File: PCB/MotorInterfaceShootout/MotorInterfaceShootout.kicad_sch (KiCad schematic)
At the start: 0 parts

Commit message: main schem start
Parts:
- added C1, C2, C3: 1uF, TJR:C_Rect_L7.3mm_W4.5_H9.5mm_P5.0mmx, symbol Device:C
- added D1, D2: LED, TSL:LED_D3.0mm, symbol 00TJR:LED
- added D3, D4, D5, D6, D7: 3V, symbol TJR:ZENER
- added J1: Motor Connector, Connector_JST:JST_XH_B6B-XH-A_1x06_P2.50mm_Vertical, symbol Connector:Conn_01x06_Pin
- added J3: Screw_Terminal_01x10, symbol connector:Screw_Terminal_01x10
- added R10, R11, R12, R7, R8, R9: 10k, TJR:R_Axial_DIN0207_L6.3mm_D2.5mm_P7.62mm_Horizontal, symbol TJR:R
- added R14, R16: 5.1k, TJR:R_Axial_DIN0207_L6.3mm_D2.5mm_P7.62mm_Horizontal, symbol TJR:R
- added R15: 47k, TJR:R_Axial_DIN0207_L6.3mm_D2.5mm_P7.62mm_Horizontal, symbol TJR:R
- added R18, R19, R20, R21: 1.3k, TJR:R_Axial_DIN0207_L6.3mm_D2.5mm_P7.62mm_Horizontal, symbol TJR:R
- added R22: 6.8k, TJR:R_Axial_DIN0207_L6.3mm_D2.5mm_P7.62mm_Horizontal, symbol TJR:R
- added R23: 1k, TJR:R_Axial_DIN0207_L6.3mm_D2.5mm_P7.62mm_Horizontal, symbol TJR:R
- added R5, R6: 330, TJR:R_Axial_DIN0207_L6.3mm_D2.5mm_P7.62mm_Horizontal, symbol TJR:R
- added U1: Pico, TJR:RPi_Pico_SMD_TH, symbol MCU_RaspberryPi_and_Boards:Pico
- added U2: OPA4197, TJR:D14_TEX, symbol Amplifier_Operational:OPA4197xPW
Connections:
- new net: R11.1, R8.2, U2.6 (-)
- new net: J3.1 (Pin_1), R21.1
- new net: R10.1, R7.2, U2.2 (-)
- new net: J3.3 (Pin_3), R22.1
- new net: J3.2 (Pin_2), R20.1
- new net: J3.4 (Pin_4), R18.1
- new net: J3.5 (Pin_5), R19.1
- new net: R12.1, R9.2, U2.9 (-)
- new net: R15.1, U2.7
- new net: R16.1, U2.8
- new net: D2.2 (A), R6.2
- new net: D1.2 (A), R5.2
- new net: R14.1, U2.1
- new net +3.3V: R7.1, R8.1, R9.1, U1.36 (3V3)
- new net +5V: U1.39 (VSYS)
- new net A: J1.5 (Pin_5), U1.4 (GPIO2)
- new net A0: D4.1 (K), R20.2
- new net A1: D6.1 (K), R21.2
- new net Analog Position: C3.1, R16.2
- new net Analog Position x10: C1.1, R14.2
- new net Analog Speed: C2.1, R15.2
- new net B: J1.6 (Pin_6), U1.5 (GPIO3)
- new net E+: J1.3 (Pin_3)
- new net E-: J1.4 (Pin_4)
- new net GND: C1.2, C2.2, C3.2, D1.1 (K), D2.1 (K), D3.2 (A), D4.2 (A), D5.2 (A), D6.2 (A), D7.2 (A), J3.9 (Pin_9), R10.2, R11.2, R12.2, R23.2, U1.12 (GPIO9), U1.18 (GND), U1.23 (GND), U1.28 (GND), U1.33 (AGND), U1.38 (GND), U1.8 (GND)
- new net M+: J1.1 (Pin_1)
- new net M-: J1.2 (Pin_2)
- new net PIN_FWD: R5.1, U1.21 (GPIO16)
- new net PIN_HOME_CMD: D5.1 (K), R18.2, U1.20 (GPIO15)
- new net PIN_HOME_LIMIT: D3.1 (K), R19.2, U1.19 (GPIO14)
- new net PIN_MOTOR_SEL: U1.17 (GPIO13)
- new net PIN_PWM_POS: J3.7 (Pin_7), U1.24 (GPIO18), U2.10 (+)
- new net PIN_PWM_POSX10: J3.6 (Pin_6), U1.26 (GPIO20), U2.3 (+)
- new net PIN_PWM_SPD: J3.8 (Pin_8), U1.25 (GPIO19), U2.5 (+)
- new net PIN_PWM_SPD_CMD: U1.27 (GPIO21)
- new net PIN_REV: R6.1, U1.22 (GPIO17)
- new net PIN_SPD_CAL_ADC: U1.32 (GPIO27_ADC1)
- new net PIN_SPD_CMD_ADC: D7.1 (K), R22.2, R23.1, U1.31 (GPIO26_ADC0)
- new net VSYS: J3.10 (Pin_10)
- no-connect marks 0 -> 21
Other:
- added sheet H-Bridge (h-bridge.kicad_sch)
- added sheet Power (power.kicad_sch)
- note added: "Main Interface Terminals Power / PLC / Limit Switch"
- note added: "Motor / Encoder Connector"
- note added: "PWM Level Transition and Integration to Analog DC Voltage 0 - 10V"
- note added: "Raspberry Pi PICO Note: Place decouple near VSYS"

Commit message: fix power
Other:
- moved on the sheet: D1, D2, R5, R6
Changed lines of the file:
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@@
 	(wire
 		(pts
-			(xy 410.21 110.49) (xy 410.21 111.76)
+			(xy 149.86 151.13) (xy 149.86 152.4)
 		)
 		(stroke
@@
 	(wire
 		(pts
-			(xy 416.56 119.38) (xy 416.56 120.65)
+			(xy 156.21 160.02) (xy 156.21 161.29)
 		)
 		(stroke
@@
 	(wire
 		(pts
-			(xy 416.56 96.52) (xy 416.56 102.87)
+			(xy 156.21 137.16) (xy 156.21 143.51)
 		)
 		(stroke
@@
 	(wire
 		(pts
-			(xy 410.21 119.38) (xy 410.21 120.65)
+			(xy 149.86 160.02) (xy 149.86 161.29)
 		)
 		(stroke
@@
 	(wire
 		(pts
-			(xy 407.67 100.33) (xy 410.21 100.33)
+			(xy 147.32 140.97) (xy 149.86 140.97)
 		)
 		(stroke
@@
 	(wire
 		(pts
-			(xy 407.67 96.52) (xy 416.56 96.52)
+			(xy 147.32 137.16) (xy 156.21 137.16)
 		)
 		(stroke
@@
 	(wire
 		(pts
-			(xy 410.21 100.33) (xy 410.21 102.87)
+			(xy 149.86 140.97) (xy 149.86 143.51)
 		)
 		(stroke
@@
 	(wire
 		(pts
-			(xy 416.56 110.49) (xy 416.56 111.76)
+			(xy 156.21 151.13) (xy 156.21 152.4)
 		)
 		(stroke
@@
 	(global_label "PIN_REV"
 		(shape input)
-		(at 407.67 96.52 180)
+		(at 147.32 137.16 180)
 		(fields_autoplaced yes)
 		(effects
@@
 		)
 		(property "Intersheetrefs" "${INTERSHEET_REFS}"
-			(at 397.0043 96.52 0)
+			(at 136.6543 137.16 0)
 			(effects
 				(font
@@
 	(global_label "PIN_FWD"
 		(shape input)
-		(at 407.67 100.33 180)
+		(at 147.32 140.97 180)
 		(fields_autoplaced yes)
 		(effects
@@
 		)
 		(property "Intersheetrefs" "${INTERSHEET_REFS}"
-			(at 396.7019 100.33 0)
+			(at 136.3519 140.97 0)
 			(effects
 				(font
@@
 				)
 				(justify left)
-				(hide yes)
 			)
 		)
@@
 				)
 				(justify left)
-				(hide yes)
 			)
 		)
@@
 	(symbol
 		(lib_id "TJR:R")
-		(at 416.56 106.68 0)
+		(at 156.21 147.32 0)
 		(unit 1)
 		(exclude_from_sim no)
@@
 		(dnp no)
 		(property "Reference" "R6"
-			(at 417.83 105.4099 0)
+			(at 157.48 146.0499 0)
 			(effects
 				(font
@@
 		)
 		(property "Value" "330"
-			(at 417.83 107.9499 0)
+			(at 157.48 148.5899 0)
 			(effects
 				(font
@@
 		)
 		(property "Footprint" "TJR:R_Axial_DIN0207_L6.3mm_D2.5mm_P7.62mm_Horizontal"
-			(at 414.782 106.68 90)
+			(at 154.432 147.32 90)
 			(effects
 				(font
@@
 		)
 		(property "Datasheet" "https://www.seielect.com/catalog/sei-cf_cfm.pdf"
-			(at 416.56 106.68 0)
+			(at 156.21 147.32 0)
 			(effects
 				(font
@@
 		)
 		(property "Description" "1/2W"
-			(at 416.56 106.68 0)
+			(at 156.21 147.32 0)
 			(effects
 				(font
@@
 		)
 		(property "digikey" "https://www.digikey.com/en/products/detail/stackpole-electronics-inc/CFM12JT47R0/1741962"
-			(at 416.56 106.68 0)
+			(at 156.21 147.32 0)
 			(effects
 				(font
@@
 		)
 		(property "Cost (ea.)" ""
-			(at 416.56 106.68 0)
+			(at 156.21 147.32 0)
 			(effects
 				(font
@@
 		)
 		(property "Notes" ""
-			(at 416.56 106.68 0)
+			(at 156.21 147.32 0)
 			(effects
 				(font
@@
 		)
 		(property "Vender Part Number" ""
-			(at 416.56 106.68 0)
+			(at 156.21 147.32 0)
 			(effects
 				(font
@@
 		)
 		(property "Vendor url" ""
-			(at 416.56 106.68 0)
+			(at 156.21 147.32 0)
 			(effects
 				(font
@@
 	(symbol
 		(lib_id "00TJR:GND")
-		(at 416.56 120.65 0)
+		(at 156.21 161.29 0)
 		(unit 1)
 		(exclude_from_sim no)
@@
 		(dnp no)
 		(property "Reference" "#PWR013"
-			(at 416.56 127 0)
+			(at 156.21 167.64 0)
 			(effects
 				(font
@@
 		)
 		(property "Value" "GND"
-			(at 416.56 124.46 0)
+			(at 156.21 165.1 0)
 			(effects
 				(font
@@
 		)
 		(property "Footprint" ""
-			(at 416.56 120.65 0)
+			(at 156.21 161.29 0)
 			(effects
 				(font
@@
 		)
 		(property "Datasheet" ""
-			(at 416.56 120.65 0)
+			(at 156.21 161.29 0)
 			(effects
 				(font
@@
 		)
 		(property "Description" ""
-			(at 416.56 120.65 0)
+			(at 156.21 161.29 0)
 			(effects
 				(font
@@
 	(symbol
 		(lib_id "TJR:R")
-		(at 410.21 106.68 0)
+		(at 149.86 147.32 0)
 		(unit 1)
 		(exclude_from_sim no)
@@
 		(dnp no)
 		(property "Reference" "R5"
-			(at 411.48 105.4099 0)
+			(at 151.13 146.0499 0)
 			(effects
 				(font
@@
 		)
 		(property "Value" "330"
-			(at 411.48 107.9499 0)
+			(at 151.13 148.5899 0)
 			(effects
 				(font
@@
 		)
 		(property "Footprint" "TJR:R_Axial_DIN0207_L6.3mm_D2.5mm_P7.62mm_Horizontal"
-			(at 408.432 106.68 90)
+			(at 148.082 147.32 90)
 			(effects
 				(font
@@
 		)
 		(property "Datasheet" "https://www.seielect.com/catalog/sei-cf_cfm.pdf"
-			(at 410.21 106.68 0)
+			(at 149.86 147.32 0)
 			(effects
 				(font
@@
 		)
 		(property "Description" "1/2W"
-			(at 410.21 106.68 0)
+			(at 149.86 147.32 0)
 			(effects
 				(font
@@
 		)
 		(property "digikey" "https://www.digikey.com/en/products/detail/stackpole-electronics-inc/CFM12JT47R0/1741962"
-			(at 410.21 106.68 0)
+			(at 149.86 147.32 0)
 			(effects
 				(font
@@
 		)
 		(property "Cost (ea.)" ""
-			(at 410.21 106.68 0)
+			(at 149.86 147.32 0)
 			(effects
 				(font
@@
 		)
 		(property "Notes" ""
-			(at 410.21 106.68 0)
+			(at 149.86 147.32 0)
 			(effects
 				(font
@@
 		)
 		(property "Vender Part Number" ""
-			(at 410.21 106.68 0)
+			(at 149.86 147.32 0)
 			(effects
 				(font
@@
 		)
 		(property "Vendor url" ""
-			(at 410.21 106.68 0)
+			(at 149.86 147.32 0)
 			(effects
 				(font
@@
 	(symbol
 		(lib_id "00TJR:LED")
-		(at 416.56 115.57 0)
+		(at 156.21 156.21 0)
 		(unit 1)
 		(exclude_from_sim no)
@@
 		(dnp no)
 		(property "Reference" "D2"
-			(at 417.068 112.268 0)
+			(at 156.718 152.908 0)
 			(effects
 				(font
@@
 		)
 		(property "Value" "LED"
-			(at 417.83 118.364 0)
+			(at 157.48 159.004 0)
 			(effects
 				(font
@@
 		)
 		(property "Footprint" "TSL:LED_D3.0mm"
-			(at 416.56 115.57 90)
+			(at 156.21 156.21 90)
 			(effects
 				(font
@@
 		)
 		(property "Datasheet" "~"
-			(at 416.56 115.57 90)
+			(at 156.21 156.21 90)
 			(effects
 				(font
@@
 		)
 		(property "Description" "Light emitting diode"
-			(at 416.56 115.57 0)
+			(at 156.21 156.21 0)
 			(effects
 				(font
@@
 		)
 		(property "Cost (ea.)" ""
-			(at 416.56 115.57 0)
+			(at 156.21 156.21 0)
 			(effects
 				(font
@@
 		)
 		(property "Notes" ""
-			(at 416.56 115.57 0)
+			(at 156.21 156.21 0)
 			(effects
 				(font
@@
 		)
 		(property "Vender Part Number" ""
-			(at 416.56 115.57 0)
+			(at 156.21 156.21 0)
 			(effects
 				(font
@@
 		)
 		(property "Vendor url" ""
-			(at 416.56 115.57 0)
+			(at 156.21 156.21 0)
 			(effects
 				(font
@@
 	(symbol
 		(lib_id "00TJR:GND")
-		(at 410.21 120.65 0)
+		(at 149.86 161.29 0)
 		(unit 1)
 		(exclude_from_sim no)
@@
 		(dnp no)
 		(property "Reference" "#PWR011"
-			(at 410.21 127 0)
+			(at 149.86 167.64 0)
 			(effects
 				(font
@@
 		)
 		(property "Value" "GND"
-			(at 410.21 124.46 0)
+			(at 149.86 165.1 0)
 			(effects
 				(font
@@
 		)
 		(property "Footprint" ""
-			(at 410.21 120.65 0)
+			(at 149.86 161.29 0)
 			(effects
 				(font
@@
 		)
 		(property "Datasheet" ""
-			(at 410.21 120.65 0)
+			(at 149.86 161.29 0)
 			(effects
 				(font
@@
 		)
 		(property "Description" ""
-			(at 410.21 120.65 0)
+			(at 149.86 161.29 0)
 			(effects
 				(font
@@
 	(symbol
 		(lib_id "00TJR:LED")
-		(at 410.21 115.57 0)
+		(at 149.86 156.21 0)
 		(unit 1)
 		(exclude_from_sim no)
@@
 		(dnp no)
 		(property "Reference" "D1"
-			(at 410.972 112.522 0)
+			(at 150.622 153.162 0)
 			(effects
 				(font
@@
 		)
 		(property "Value" "LED"
-			(at 411.226 118.11 0)
+			(at 150.876 158.75 0)
 			(effects
 				(font
@@
 		)
 		(property "Footprint" "TSL:LED_D3.0mm"
-			(at 410.21 115.57 90)
+			(at 149.86 156.21 90)
 			(effects
 				(font
@@
 		)
 		(property "Datasheet" "~"
-			(at 410.21 115.57 90)
+			(at 149.86 156.21 90)
 			(effects
 				(font
@@
 		)
 		(property "Description" "Light emitting diode"
-			(at 410.21 115.57 0)
+			(at 149.86 156.21 0)
 			(effects
 				(font
@@
 		)
 		(property "Cost (ea.)" ""
-			(at 410.21 115.57 0)
+			(at 149.86 156.21 0)
 			(effects
 				(font
@@
 		)
 		(property "Notes" ""
-			(at 410.21 115.57 0)
+			(at 149.86 156.21 0)
 			(effects
 				(font
@@
 		)
 		(property "Vender Part Number" ""
-			(at 410.21 115.57 0)
+			(at 149.86 156.21 0)
 			(effects
 				(font
@@
 		)
 		(property "Vendor url" ""
-			(at 410.21 115.57 0)
+			(at 149.86 156.21 0)
 			(effects
 				(font

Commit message: working on h-bridge logic
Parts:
- removed R10, R11, R12, R7, R8, R9: 10k, TJR:R_Axial_DIN0207_L6.3mm_D2.5mm_P7.62mm_Horizontal, symbol TJR:R
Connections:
- net COMP_THRES: now reaches U2.6 (-)
- net COMP_THRES: now also U2.2 (-), U2.9 (-)

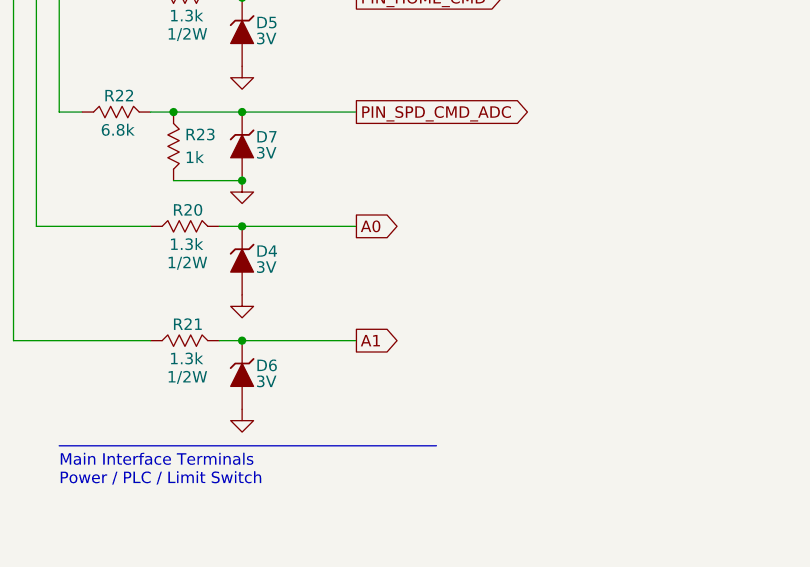
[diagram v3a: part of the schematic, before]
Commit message: fix h-bridge pwm logic
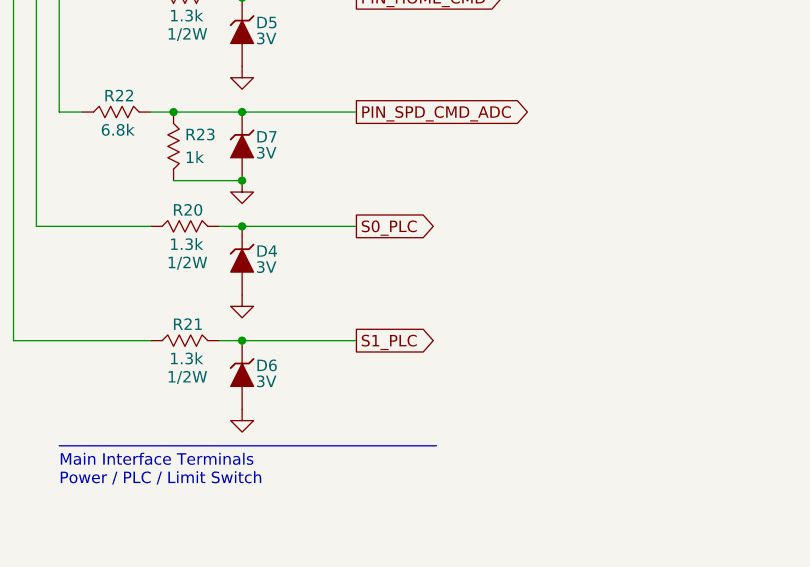
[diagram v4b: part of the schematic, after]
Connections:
- net A0 renamed S0_PLC
- net A1 renamed S1_PLC
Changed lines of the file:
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@@
 		)
 	)
-	(global_label "A1"
+	(global_label "S1_PLC"
 		(shape output)
 		(at 85.09 179.07 0)
@@
 		)
 		(property "Intersheetrefs" "${INTERSHEET_REFS}"
-			(at 90.3733 179.07 0)
+			(at 95.0299 179.07 0)
 			(effects
 				(font
@@
 		)
 	)
-	(global_label "A0"
+	(global_label "S0_PLC"
 		(shape output)
 		(at 85.09 166.37 0)
@@
 		)
 		(property "Intersheetrefs" "${INTERSHEET_REFS}"
-			(at 90.3733 166.37 0)
-			(effects
-				(font
+			(at 95.0299 166.37 0)
+			(effects
+				(font

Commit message: ready for cleanup and layout
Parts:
- added JP1: Jumper_2_Open, symbol jumper:Jumper_2_Open
- added R?: 10k, symbol device:R_Potentiometer_US
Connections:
- net +3.3V: now also U1.35 (ADC_VREF), R?.1
- net GND: now also JP1.1 (A), R?.3
- net PIN_MOTOR_SEL: no longer names the net of U1.17 (GPIO13)
- net PIN_MOTOR_SEL: now also JP1.2 (B)
- net PIN_SPD_CAL_ADC: no longer names the net of U1.32 (GPIO27_ADC1)
- net PIN_SPD_CAL_ADC: now also R?.2
- no-connect marks 21 -> 20

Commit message: working on part source
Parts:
- added D8, D9: 3V, symbol TJR:ZENER
- added R13, R14: 6.8k, symbol TJR:R
- D1: renamed from D3; digikey (none) -> https://www.digikey.com/en/products/detail/central-semicond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
- D2: renamed from D5; digikey (none) -> https://www.digikey.com/en/products/detail/central-semicond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
- D3: renamed from D7; digikey (none) -> https://www.digikey.com/en/products/detail/central-semicond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
- D4: digikey (none) -> https://www.digikey.com/en/products/detail/central-semicond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
- D5: renamed from D6; digikey (none) -> https://www.digikey.com/en/products/detail/central-semicond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
- D6: renamed from D1; value LED -> Red; footprint TSL:LED_D3.0mm -> (none); digikey (none) -> https://www.digikey.com/en/products/detail/ams-osram-usa-in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
- D7: renamed from D2; value LED -> Green; footprint TSL:LED_D3.0mm -> (none); digikey (none) -> https://www.digikey.com/en/products/detail/ams-osram-usa-in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
- R1: renamed from R22; footprint TJR:R_Axial_DIN0207_L6.3mm_D2.5mm_P7.62mm_Horizontal -> (none)
- R10: renamed from R14; footprint TJR:R_Axial_DIN0207_L6.3mm_D2.5mm_P7.62mm_Horizontal -> (none)
- R11: renamed from R15; footprint TJR:R_Axial_DIN0207_L6.3mm_D2.5mm_P7.62mm_Horizontal -> (none)
- R12: renamed from R16; footprint TJR:R_Axial_DIN0207_L6.3mm_D2.5mm_P7.62mm_Horizontal -> (none)
- R2: renamed from R23; footprint TJR:R_Axial_DIN0207_L6.3mm_D2.5mm_P7.62mm_Horizontal -> (none)
- R3: renamed from R19; value 1.3k -> 6.8k; footprint TJR:R_Axial_DIN0207_L6.3mm_D2.5mm_P7.62mm_Horizontal -> (none); digikey https://www.digikey.com/en/products/detail/stackpole-electronics-inc/RNCP1206FTD1K30/2240340 -> https://www.digikey.com/en/products/detail/stackpole-electronics-inc/RMCF0805JT6K80/1757931
- R4: renamed from R18; value 1.3k -> 6.8k; footprint TJR:R_Axial_DIN0207_L6.3mm_D2.5mm_P7.62mm_Horizontal -> (none); digikey https://www.digikey.com/en/products/detail/stackpole-electronics-inc/RNCP1206FTD1K30/2240340 -> https://www.digikey.com/en/products/detail/stackpole-electronics-inc/RMCF0805JT6K80/1757931
- R5: renamed from R20; value 1.3k -> 6.8k; footprint TJR:R_Axial_DIN0207_L6.3mm_D2.5mm_P7.62mm_Horizontal -> (none); digikey https://www.digikey.com/en/products/detail/stackpole-electronics-inc/RNCP1206FTD1K30/2240340 -> https://www.digikey.com/en/products/detail/stackpole-electronics-inc/RMCF0805JT6K80/1757931
- R6: renamed from R21; value 1.3k -> 6.8k; footprint TJR:R_Axial_DIN0207_L6.3mm_D2.5mm_P7.62mm_Horizontal -> (none); digikey https://www.digikey.com/en/products/detail/stackpole-electronics-inc/RNCP1206FTD1K30/2240340 -> https://www.digikey.com/en/products/detail/stackpole-electronics-inc/RMCF0805JT6K80/1757931
- R7: renamed from R?; digikey (none) -> https://www.digikey.com/en/products/detail/stackpole-electr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
- R8: renamed from R5; footprint TJR:R_Axial_DIN0207_L6.3mm_D2.5mm_P7.62mm_Horizontal -> (none)
- R9: renamed from R6; footprint TJR:R_Axial_DIN0207_L6.3mm_D2.5mm_P7.62mm_Horizontal -> (none)
- renumbered J3 to J1, J1 to J2
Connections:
- net A: now also D8.1 (K), R13.2; no longer J2.5 (Pin_5)
- net B: now also D9.1 (K), R14.2; no longer J2.6 (Pin_6)
- net GND: now also U1.13 (GND), U1.3 (GND), D8.2 (A), D9.2 (A); no longer U1.12 (GPIO9)
- new net: J2.5 (Pin_5), R13.1
- new net: J2.6 (Pin_6), R14.1
- no-connect marks 20 -> 19
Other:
- moved on the sheet: D6, D7, R8, R9
